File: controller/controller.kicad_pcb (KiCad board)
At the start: 2 copper layers, 90 x 60 mm, 20 parts, among them J2 Conn_01x03_Socket, J3 WAGO 236-402, J4 WAGO 236-402, J5 WAGO 236-404, Q1 2N2222

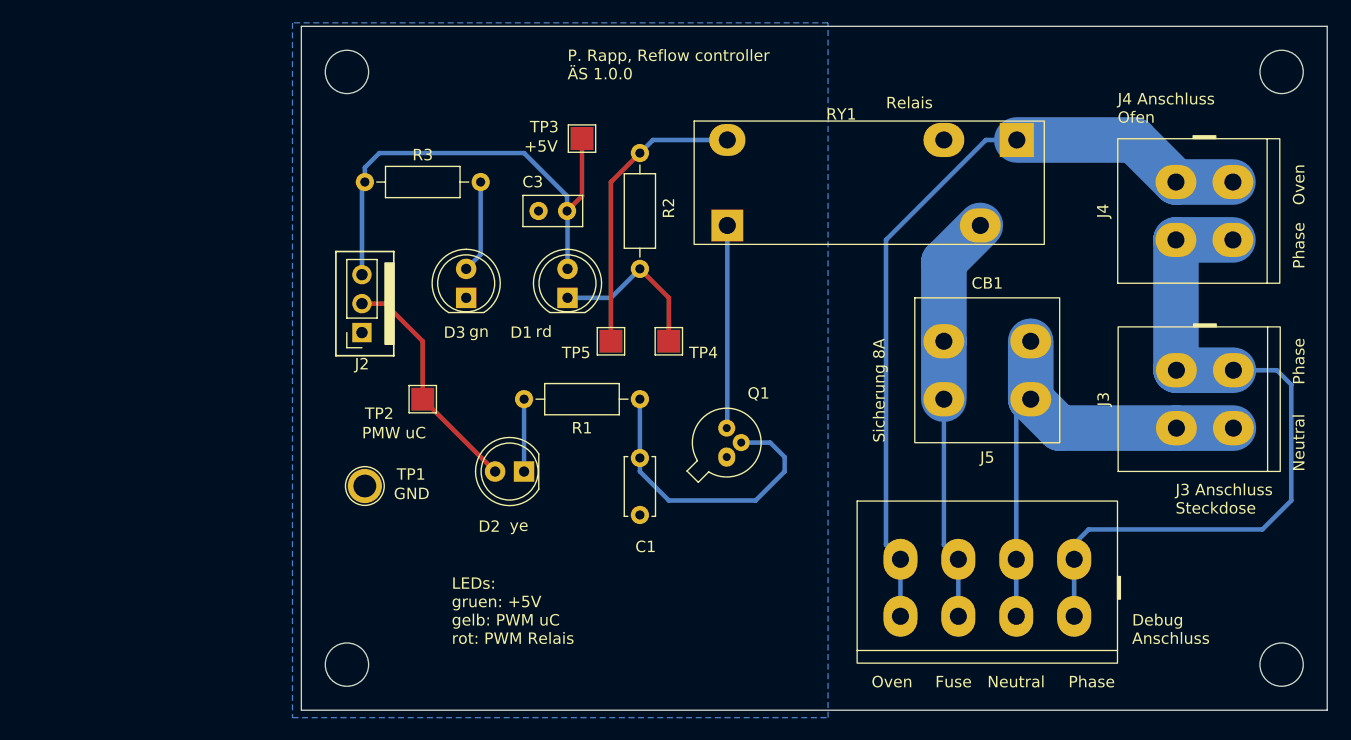
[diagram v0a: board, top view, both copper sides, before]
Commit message: Incorporated changes to the reflow controller schematic (v1.0.0 to v1.0.1)
Also incorporated some changes to the board, but did not place
and route the two additional resistors.
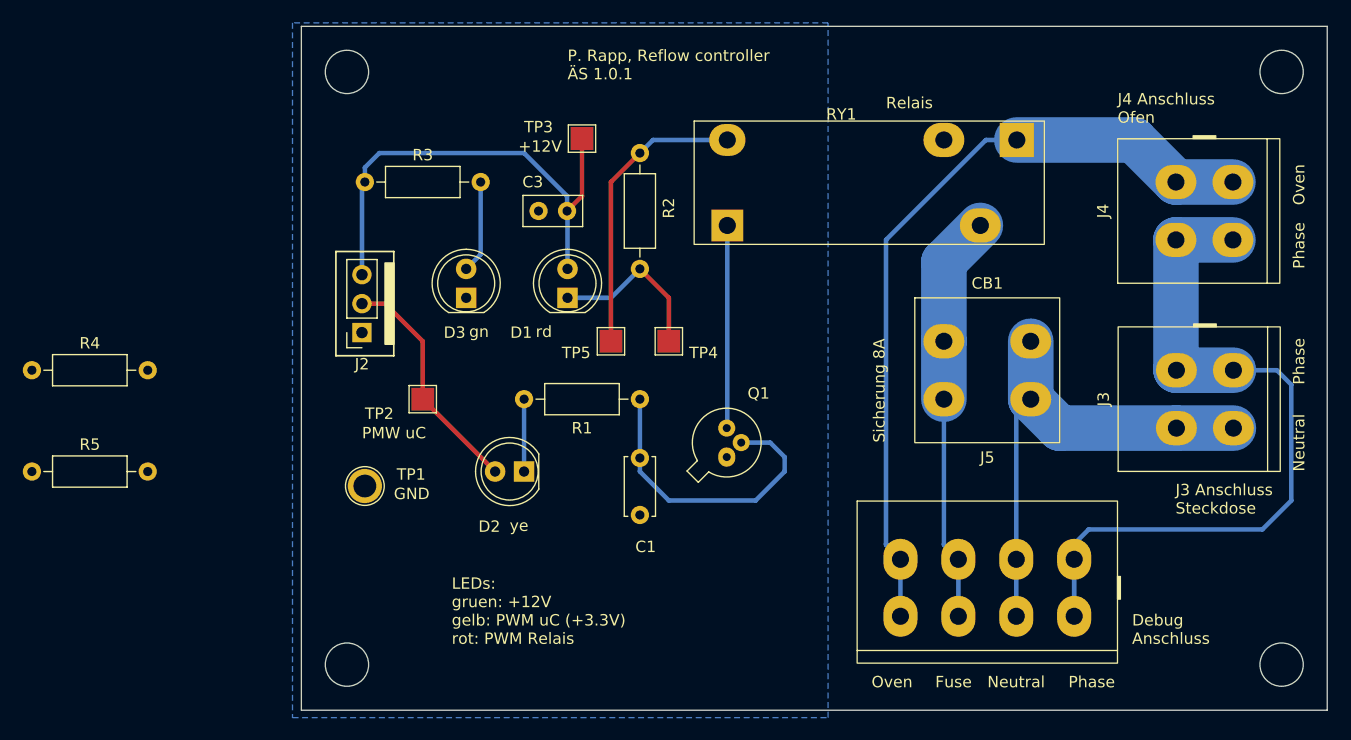
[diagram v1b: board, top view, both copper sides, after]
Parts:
- added R4: 47R, Resistor_THT:R_Axial_DIN0207_L6.3mm_D2.5mm_P10.16mm_Horizontal, F.Cu at (86.4, 90.2)
- added R5: 47R, Resistor_THT:R_Axial_DIN0207_L6.3mm_D2.5mm_P10.16mm_Horizontal, F.Cu at (86.4, 99.1)
- R1: value 1k -> 100R
- R2: value 22R -> 150R
- R3: value 1k -> 3.9k
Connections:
- net +5V renamed +12V
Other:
- board text added: "+12V"
- board text added: "LEDs: gruen: +12V gelb: PWM uC (+3.3V) rot: PWM Relais"
- board text added: "P. Rapp, Reflow controller ÄS 1.0.1"
- board text removed: "+5V"
- board text removed: "LEDs: gruen: +5V gelb: PWM uC rot: PWM Relais"
- board text removed: "P. Rapp, Reflow controller ÄS 1.0.0"
